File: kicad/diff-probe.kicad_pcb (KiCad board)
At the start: 2 copper layers, 49.2 x 20.5 mm, 44 parts, among them J1 HEADER-1X2CARD-EDGE, J3 Molex 502494-0470, J4 901-10511-3, U1 OPA847xDBV, U2 OPA847xDBV, U3 AP3211K, U4 AP3211K

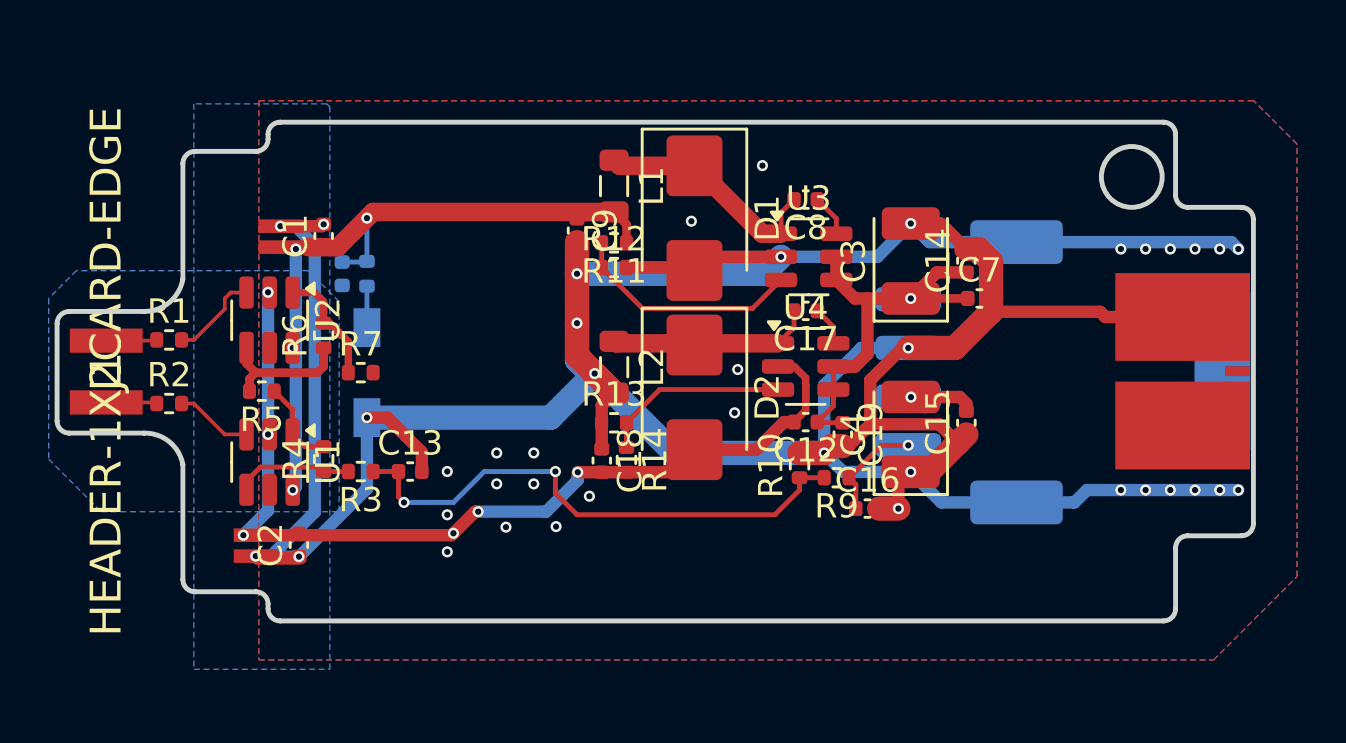
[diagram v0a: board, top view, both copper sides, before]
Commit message: 1. Update project regarding to the clean up the rules for the https://jlcpcb.com/ 2. Make the output as Co-planar Wave-guide 50 Ohm 3. Trim the differential input length, and width
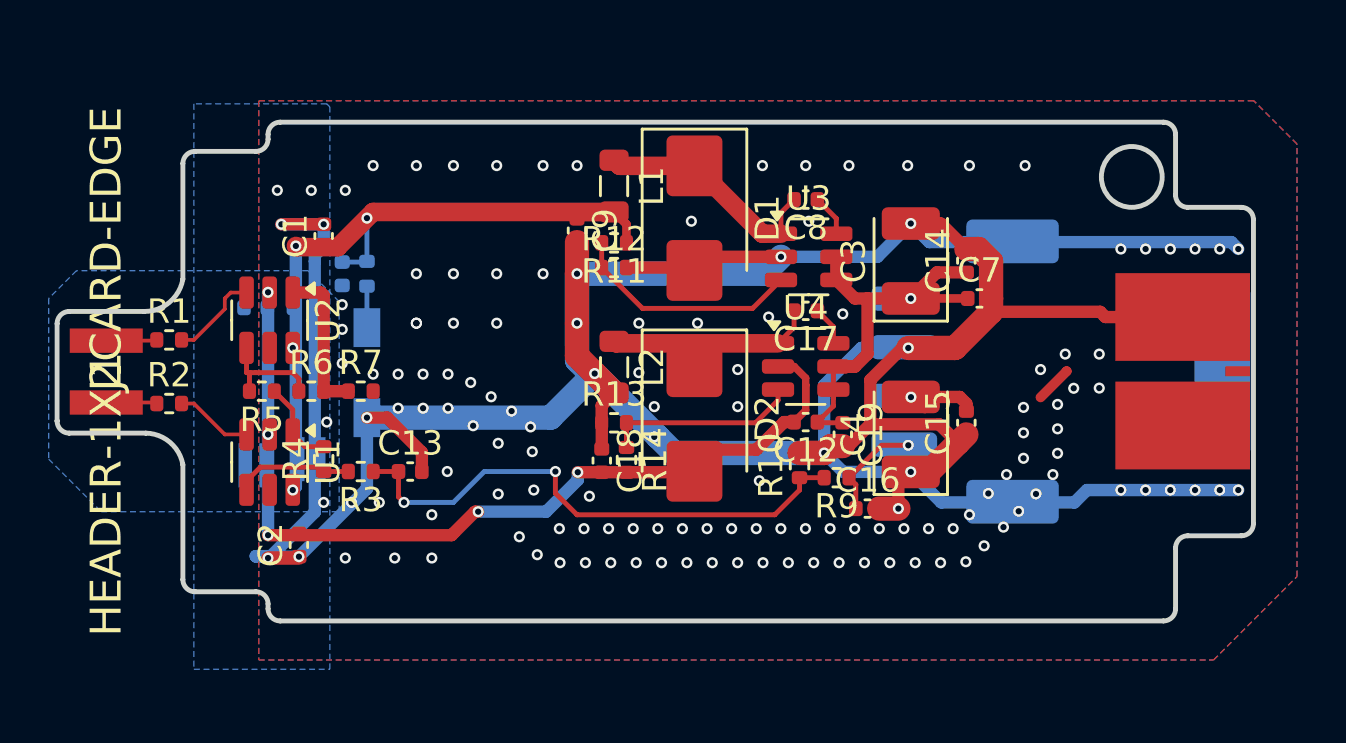
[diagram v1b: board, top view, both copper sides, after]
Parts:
- added C20: 100nF, Capacitor_SMD:C_0402_1005Metric, B.Cu at (134.9, 95.4)
- added C21: 100nF, Capacitor_SMD:C_0402_1005Metric, B.Cu at (132.8, 95.4)
- C5, C6: moved to B.Cu
- moved C6 9.22 mm to (135.0, 101.6), turned to 0 degrees
- moved C5 3.30 mm to (132.8, 101.9), turned to 0 degrees
- moved R6 2.34 mm to (135.1, 98.8), turned to 0 degrees
- moved D2 0.89 mm to (150.9, 99.9)
- moved R7 0.76 mm to (137.2, 98.8)
- moved J3 0.17 mm to (162.0, 98.0)
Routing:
- net /Power_supply/V-: track 55.0 -> 51.9 mm, vias 6 -> 5
- net /OUT: track 4.92 -> 6.27 mm
- net /Power_supply/V+: track 41.0 -> 39.8 mm
- net Net-(U2--): track 5.70 -> 4.55 mm
- net /OutPad: track 45.9 -> 45.0 mm
- net GND: track 162.9 -> 162.0 mm, vias 40 -> 145
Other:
- outline, holes or cut-outs redrawn
- board text added: "0"
- board text added: "0 mm"
- board text added: "0.01 mm"
- board text added: "0.02"
- board text added: "0.035 mm"
- board text added: "1"
- board text added: "1.51 mm"
- board text added: "3.3"
- board text added: "4.5"
- board text added: "B.Cu"
- board text added: "B.Mask"
- board text added: "B.Paste"
- board text added: "B.Silkscreen"
- board text added: "Bottom Silk Screen"
- board text added: "Bottom Solder Mask"
- board text added: "Bottom Solder Paste"
- board text added: "Color"
- board text added: "Dielectric"
- board text added: "Direct Printing"
- board text added: "Dry Film"
- board text added: "Epsilon R"
- board text added: "F.Cu"
- board text added: "F.Mask"
- board text added: "F.Paste"
- board text added: "F.Silkscreen"
- board text added: "FR4"
- board text added: "Green"
- board text added: "Layer Name"
- board text added: "Loss Tangent"
- board text added: "Material"
- board text added: "Not specified"
- board text added: "Thickness (mm)"
- board text added: "Top Silk Screen"
- board text added: "Top Solder Mask"
- board text added: "Top Solder Paste"
- board text added: "Type"
- board text added: "White"
- board text added: "copper"
- board text added: "core"

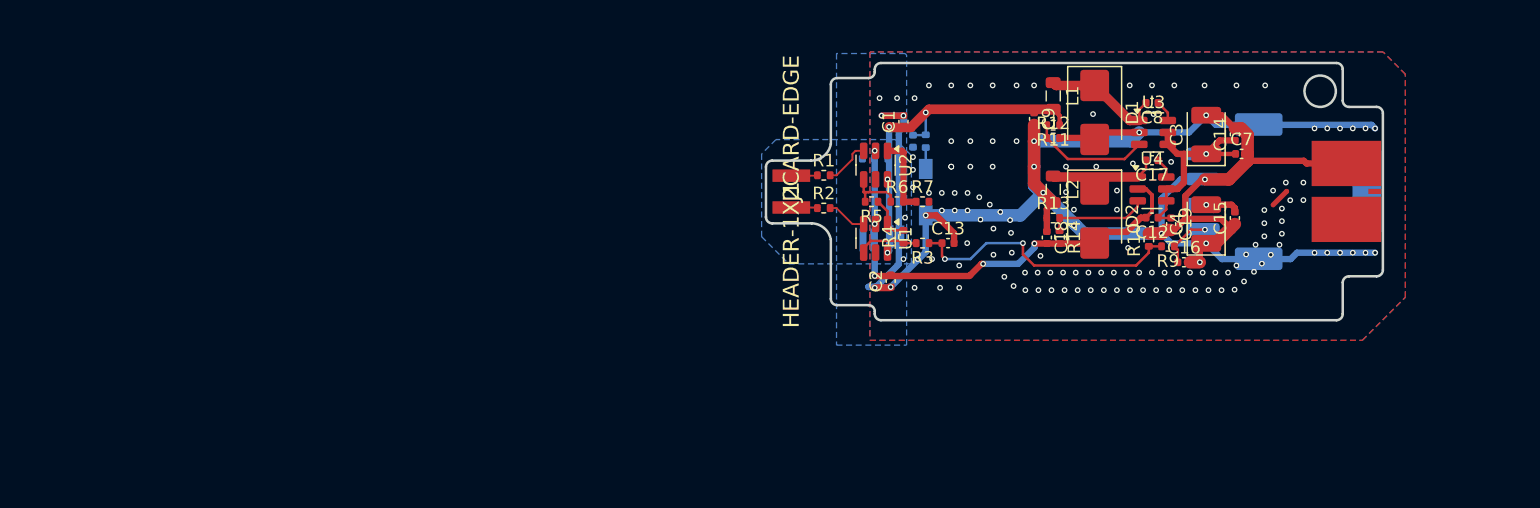
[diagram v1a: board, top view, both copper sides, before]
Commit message: Update Autoprobe project to the Kicad 9.xx Add some Bin files for the EEPROM data add some documentation files
Update the High speed diff probe Kicad data
change the silkscreen - more reasonable position
Add the Project Name, an revision on the PCB board.
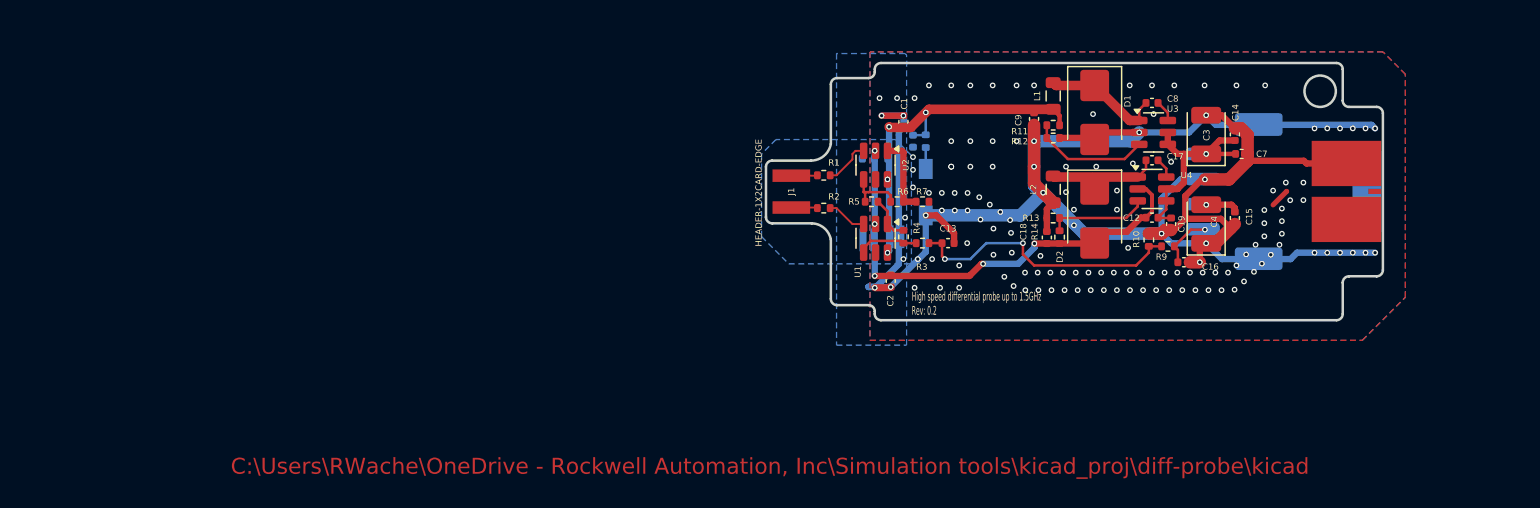
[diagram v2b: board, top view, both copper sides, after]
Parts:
- added G_Bandwidth : LOGO, LOGO, B.Cu at (148.5, 95.1)
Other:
- board text added: "${TITLE} Rev: ${REVISION}"
- board text added: "C:\Users\RWache\OneDrive - Rockwell Automation, Inc\Simulation tools\kicad_proj\diff-probe\kicad"
